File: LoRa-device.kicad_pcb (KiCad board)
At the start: 2 copper layers, 86.4 x 50.8 mm, 90 parts, among them J1 USB_C_Receptacle_USB2.0_14P, J2 Conn_01x02_Pin, J3 Conn_01x12_Pin, J4 Conn_01x14_Pin, J6 Conn_01x04_Pin, Q1 AO3401A, Q2 S8050, U1 ESP32-S3, U2 W25Q128JVS, U3 MCP73831-2-OT, U4 AMS1117-3.3, U5 Ai-Thinker-Ra-01, U6 BME280, U7 L70-R, Y1 32.768 kHz, Y2 40MHz(10ppm)

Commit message: First routing
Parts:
- removed C1: 100nF, PCM_JLCPCB:C_0402
- removed C5, C9: 15pF, Capacitor_SMD:C_0402_1005Metric
- removed U6: BME280, PCM_JLCPCB:Bosch_LGA-8_2.5x2.5mm_P0.65mm_ClockwisePinNumbering
- added DNP4: ~, Capacitor_SMD:C_0402_1005Metric, F.Cu at (163.7, 75.8)
- added DNP5: ~, Capacitor_SMD:C_0402_1005Metric, F.Cu at (176.2, 119.8)
- added Q3: AO3401A, Package_TO_SOT_SMD:SOT-23, F.Cu at (112.5, 113.7)
- added R7: 100kΩ, PCM_JLCPCB:R_0402, F.Cu at (115.2, 113.7)
- added SW1: SW_Nidec_CAS-120A1, Connector_PinSocket_2.54mm:PinSocket_1x03_P2.54mm_Vertical, F.Cu at (185.7, 114.9)
- DNP2, DNP3: value 15pF -> ~
- moved Q2 27.4 mm to (173.5, 103.7)
- moved D5 27.4 mm to (179.5, 103.7)
- moved R5 27.4 mm to (170.4, 103.3)
- moved BZ1 26.1 mm to (176.6, 111.7)
- moved DNP3 16.0 mm to (157.2, 114.6), turned to 180 degrees
- moved L4 15.6 mm to (160.7, 117.0), turned to 180 degrees
- moved R4 15.6 mm to (159.6, 114.6)
- moved R6 13.8 mm to (161.4, 115.0), turned to 90 degrees
- moved R3 12.6 mm to (165.7, 114.9), turned to -90 degrees
- moved DNP2 12.4 mm to (163.7, 78.5)
- moved L1 12.3 mm to (166.2, 77.2)
- moved U7 6.97 mm to (161.4, 107.2), turned to -90 degrees
- moved R25 4.97 mm to (116.7, 82.1), turned to 180 degrees
- moved R24 4.27 mm to (141.2, 89.7), turned to 0 degrees
- moved J3 4.25 mm to (141.6, 121.8)
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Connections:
- C7 pad 1: VSYS -> VSYS_SW
- J3 pad 3: VDD_CPU -> GND
- J3 pad 4: GND -> IO37
- U4 pad 3: VSYS -> VSYS_SW
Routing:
- net Net-(Q3-G): track 0.00 -> 87.5 mm, vias 0 -> 2
- net IO7: track 0.00 -> 85.9 mm, vias 0 -> 4
- net IO35: track 0.00 -> 64.4 mm, vias 0 -> 4
- net IO21: track 0.00 -> 57.4 mm, vias 0 -> 2
- net IO36: track 0.00 -> 54.9 mm, vias 0 -> 4
- net IO34: track 0.00 -> 41.8 mm, vias 0 -> 2
- net RX: track 0.00 -> 41.8 mm, vias 0 -> 4
- net VSYS_SW: track 0.00 -> 34.9 mm, vias 0 -> 2
- net IO14/SCK: track 171.6 -> 141.0 mm, vias 10 -> 9
- net IO46: track 80.1 -> 50.1 mm, vias 9 -> 3
- net IO0: track 14.7 -> 41.4 mm, vias 2 -> 4
- net IO5: track 40.7 -> 65.1 mm
- net Net-(U5-ANT): track 29.8 -> 5.93 mm, vias 2 -> 0
- net SPICS0: track 0.00 -> 23.8 mm, vias 0 -> 4
- net IO39: track 56.3 -> 77.0 mm, vias 2 -> 3
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
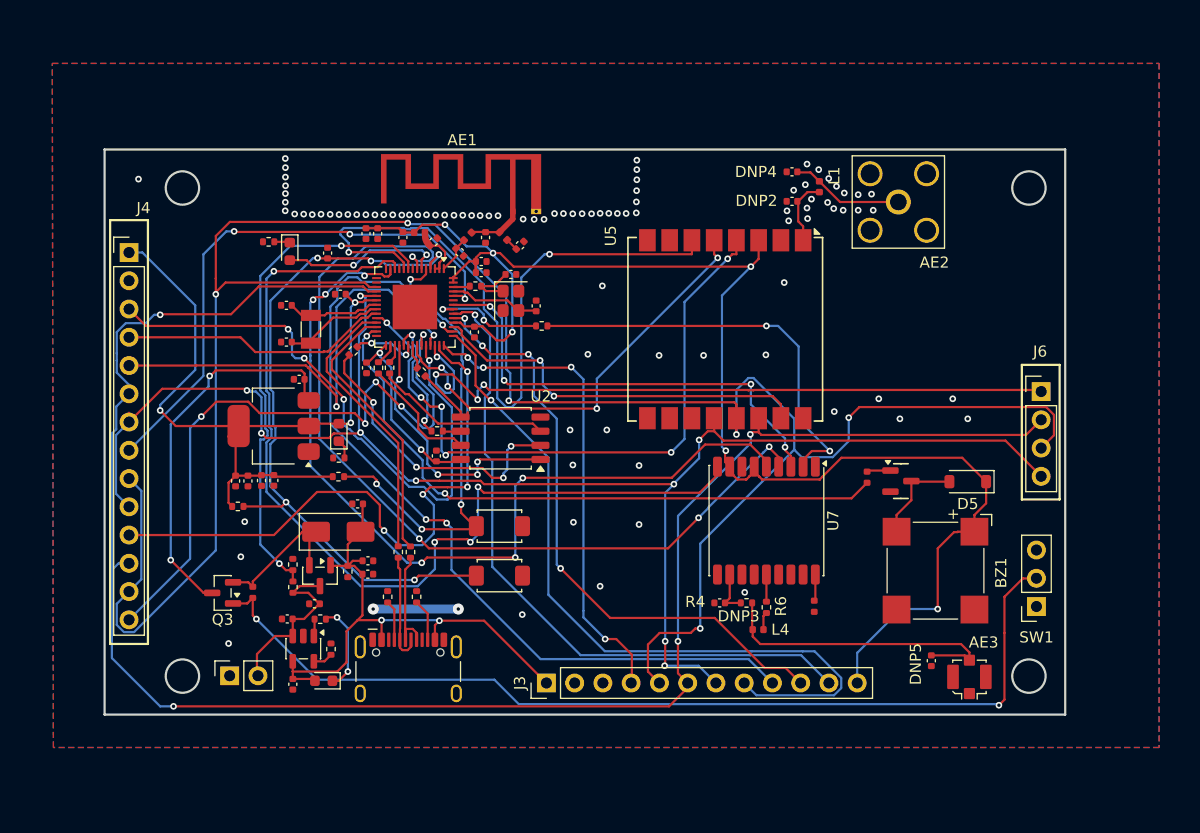
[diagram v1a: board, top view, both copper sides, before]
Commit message: Completed routing
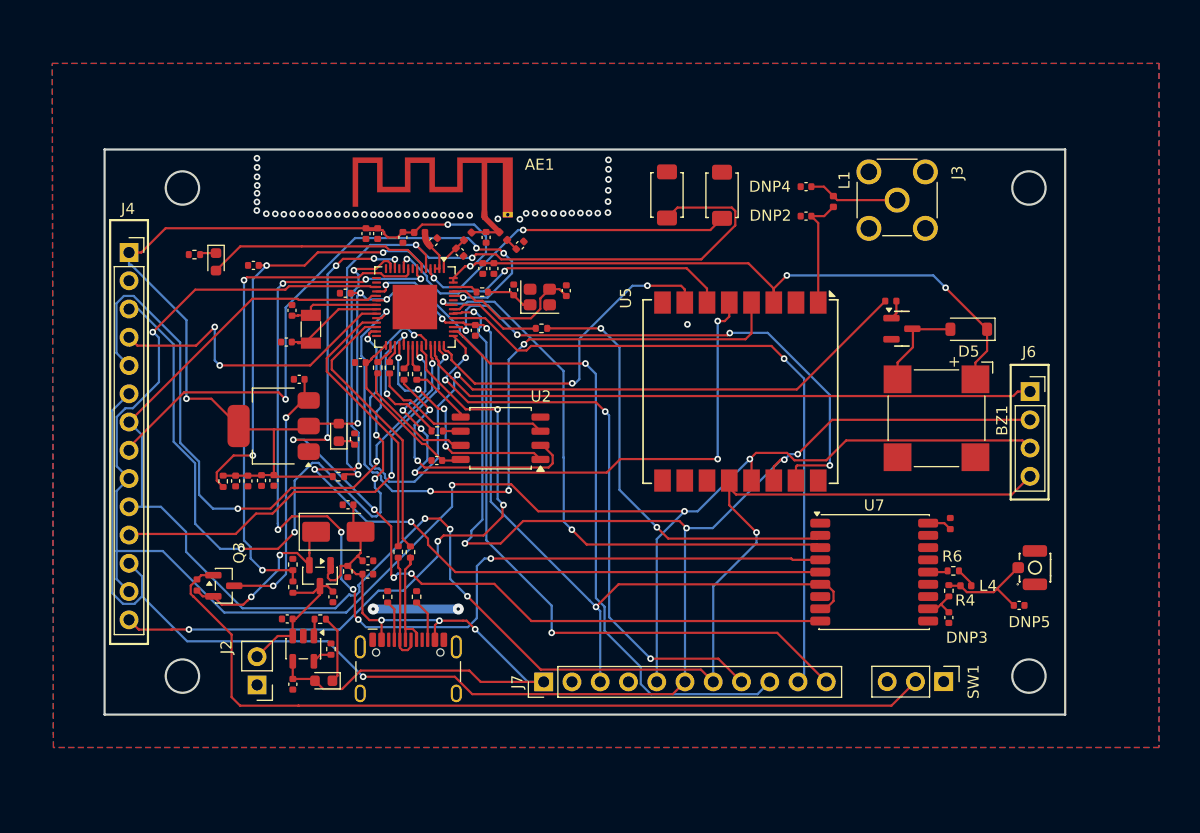
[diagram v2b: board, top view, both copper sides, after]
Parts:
- removed AE2: Antenna, Connector_Coaxial:SMA_Amphenol_132203-12_Horizontal
- removed AE3: Antenna, Connector_Coaxial:U.FL_Molex_MCRF_73412-0110_Vertical
- removed Flash1, Reset1: Tactile Button, 160gf, PCM_JLCPCB:SW_TS-1088-AR02016
- added FLASH1: Tactile Button, 160gf, PCM_JLCPCB:SW_TS-1088-AR02016, F.Cu at (152.5, 77.9)
- added J5: U.FL, PCM_JLCPCB:IPEX-SMD_BWIPX-1-001E, F.Cu at (184.8, 111.4)
- added J7: Conn_01x11_Pin, Connector_PinHeader_2.54mm:PinHeader_1x11_P2.54mm_Vertical, F.Cu at (141.4, 121.7)
- added RESET1: Tactile Button, 160gf, PCM_JLCPCB:SW_TS-1088-AR02016, F.Cu at (157.4, 78.0)
- J2: footprint Connector_PinSocket_2.54mm:PinSocket_1x02_P2.54mm_Vertical -> Connector_PinHeader_2.54mm:PinHeader_1x02_P2.54mm_Vertical
- J3: value Conn_01x12_Pin -> Conn_Coaxial; footprint Connector_PinHeader_2.54mm:PinHeader_1x12_P2.54mm_Vertical -> Connector_Coaxial:SMA_Molex_73251-2200_Horizontal
- J4: footprint Connector_PinHeader_2.54mm:PinHeader_1x14_P2.54mm_Vertical -> Connector_PinSocket_2.54mm:PinSocket_1x14_P2.54mm_Vertical
- J6: footprint Connector_PinHeader_2.54mm:PinHeader_1x04_P2.54mm_Vertical -> Connector_PinSocket_2.54mm:PinSocket_1x04_P2.54mm_Vertical
- SW1: footprint Connector_PinSocket_2.54mm:PinSocket_1x03_P2.54mm_Vertical -> Connector_PinHeader_2.54mm:PinHeader_1x03_P2.54mm_Vertical
- moved J3 53.7 mm to (173.2, 78.4), turned to 0 degrees
- moved DNP3 20.6 mm to (177.8, 115.9), turned to -90 degrees
- moved L4 19.1 mm to (179.3, 113.1)
- moved R4 18.2 mm to (177.8, 113.5), turned to 90 degrees
- moved R6 17.1 mm to (178.2, 111.7), turned to 180 degrees
- moved R5 16.0 mm to (172.6, 87.5), turned to 0 degrees
- moved R3 14.3 mm to (177.9, 107.5), turned to 90 degrees
- moved BZ1 13.7 mm to (176.7, 98.0)
- moved D5 13.7 mm to (179.6, 90.0)
- moved Q2 13.7 mm to (173.6, 90.0)
- moved U7 10.7 mm to (171.1, 111.8), turned to 0 degrees
- moved SW1 10.7 mm to (177.3, 121.7), turned to -90 degrees
- moved DNP5 9.33 mm to (184.1, 114.8), turned to 0 degrees
- moved R25 6.77 mm to (110.0, 83.3)
- moved C15 6.76 mm to (115.3, 84.3), turned to 180 degrees
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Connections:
- DNP4 pad 1: Net-(AE2-FEED) -> Net-(J3-In)
- J3 pad 1: 5V -> Net-(J3-In)
- L1 pad 2: Net-(AE2-FEED) -> Net-(J3-In)
- U5 pad 7: unconnected-(U5-DIO2-Pad7) -> IO37
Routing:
- net IO12/MISO: track 205.7 -> 161.9 mm, vias 6 -> 4
- net IO5: track 65.1 -> 32.5 mm
- net VDD_CPU: track 203.5 -> 233.3 mm, vias 9 -> 11
- net IO0: track 41.4 -> 68.6 mm, vias 4 -> 3
- net IO39: track 77.0 -> 56.4 mm, vias 3 -> 1
- net IO2: track 80.4 -> 98.6 mm, vias 4 -> 8
- net Net-(J5-In): track 27.4 -> 9.53 mm
- net IO48: track 39.6 -> 57.0 mm, vias 4 -> 6
- net IO34: track 41.8 -> 59.2 mm, vias 2 -> 3
- net IO33: track 53.3 -> 69.2 mm, vias 4 -> 5
- net IO40: track 35.0 -> 50.2 mm, vias 2 -> 4
- net IO36: track 54.9 -> 39.7 mm, vias 4 -> 2
- net IO13/MOSI: track 166.2 -> 181.2 mm, vias 4 -> 6
- net IO21: track 57.4 -> 71.4 mm
- net IO14/SCK: track 141.0 -> 154.6 mm, vias 9 -> 4
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
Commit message: Major rerouting and ESD protection for USB port
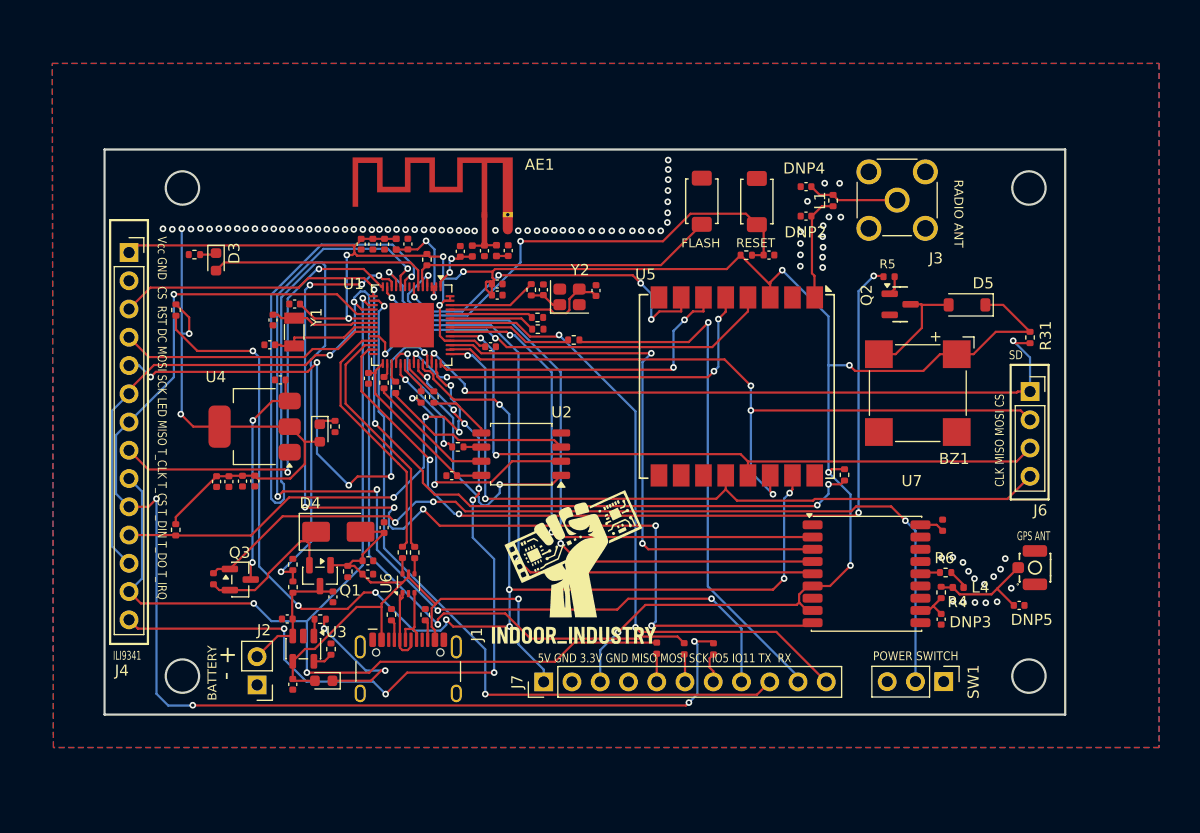
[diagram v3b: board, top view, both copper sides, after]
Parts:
- removed C36: 10uF, Capacitor_SMD:C_0402_1005Metric
- added C1: 1uF, Capacitor_SMD:C_0402_1005Metric, F.Cu at (118.8, 121.9)
- added G***: LOGO, LOGO, F.Cu at (144.1, 112.7)
- added R10: 10K, Resistor_SMD:R_0402_1005Metric, F.Cu at (168.4, 103.1)
- added R11: 10K, Resistor_SMD:R_0402_1005Metric, F.Cu at (108.3, 108.0)
- added R13: 10K, Resistor_SMD:R_0402_1005Metric, F.Cu at (108.3, 88.3)
- added R31: 10K, Resistor_SMD:R_0402_1005Metric, F.Cu at (185.1, 90.7)
- added R32: 10Ω, PCM_JLCPCB:R_0402, F.Cu at (151.5, 118.7)
- added R33: 10Ω, PCM_JLCPCB:R_0402, F.Cu at (154.0, 118.7)
- added R34: 10Ω, PCM_JLCPCB:R_0402, F.Cu at (156.6, 118.7)
- added R8: 10K, Resistor_SMD:R_0402_1005Metric, F.Cu at (140.8, 90.0)
- added R9: 10K, Resistor_SMD:R_0402_1005Metric, F.Cu at (140.8, 88.9)
- added U6: USBLC6-2P6, Package_TO_SOT_SMD:SOT-666, F.Cu at (129.2, 112.8)
- DNP1: value 15pF -> ~
- L1: value 4.7nH -> 0R; footprint Inductor_SMD:L_0402_1005Metric -> Resistor_SMD:R_0402_1005Metric
- U3: value MCP73831-2-OT -> TP4055
- moved R22 51.2 mm to (159.6, 83.3), turned to 180 degrees
- moved C15 46.4 mm to (161.6, 83.3), turned to 0 degrees
- moved R21 21.1 mm to (130.9, 83.7), turned to -90 degrees
- moved C10 4.65 mm to (119.0, 87.7)
- moved R23 4.41 mm to (140.3, 86.5), turned to 90 degrees
- moved C22 3.83 mm to (127.0, 107.8), turned to 90 degrees
- moved FLASH1 3.18 mm to (155.6, 78.5)
- moved RESET1 3.18 mm to (160.5, 78.5)
- moved R24 3.08 mm to (144.1, 91.0)
- moved BZ1 2.82 mm to (175.0, 95.7)
- moved C40 2.72 mm to (137.2, 86.9), turned to 0 degrees
- moved C33 2.67 mm to (146.1, 86.5)
- moved C4 2.67 mm to (141.3, 86.5)
- moved Y2 2.67 mm to (143.7, 87.1)
- moved R26 2.57 mm to (131.5, 96.1)
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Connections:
- C17 pad 1: VDD_CPU -> GND
- C20 pad 1: VDD_CPU -> GND
- C3 pad 1: VDD_CPU -> GND
- C35 pad 1: VDD_CPU -> GND
- D2 pad 2: VDD_CPU -> GND
- J1 pad A6: USB_D+ -> Net-(J1-D+-PadA6)
- J1 pad A7: USB_D- -> Net-(J1-D--PadA7)
- J1 pad B6: USB_D+ -> Net-(J1-D+-PadA6)
- J1 pad B7: USB_D- -> Net-(J1-D--PadA7)
- J4 pad 10: IO14/SCK -> SCKB
- J4 pad 12: IO13/MOSI -> MOSIB
- J4 pad 13: IO12/MISO -> MISOB
- J4 pad 3: IO33 -> IO10
- J4 pad 6: IO13/MOSI -> MOSIB
- J4 pad 7: IO14/SCK -> SCKB
- J4 pad 8: IO46 -> IO9
- J4 pad 9: IO12/MISO -> MISOB
- J6 pad 2: IO13/MOSI -> MOSIA
- J6 pad 3: IO12/MISO -> MISOA
- J6 pad 4: IO14/SCK -> SCKA
- J7 pad 10: IO41 -> TX
- J7 pad 11: IO42 -> RX
- J7 pad 5: IO12/MISO -> Net-(J7-Pin_5)
- J7 pad 6: IO13/MOSI -> Net-(J7-Pin_6)
- J7 pad 7: IO14/SCK -> Net-(J7-Pin_7)
- J7 pad 8: IO38 -> IO5
- J7 pad 9: IO39 -> IO11
- R18 pad 1: USB_D+ -> Net-(R18-Pad1)
- R2 pad 1: USB_D- -> Net-(R2-Pad1)
- U1 pad 17: IO12/MISO -> MISOB
- U1 pad 18: IO13/MOSI -> MOSIB
- U1 pad 19: IO14/SCK -> SCKB
- U1 pad 43: IO38 -> SCKA
- U1 pad 44: IO39 -> MOSIA
- U1 pad 47: IO41 -> MISOA
- U1 pad 8: IO3 -> unconnected-(U1-GPIO3-Pad8)
- U4 pad 2: VDD_CPU -> GND
- U5 pad 12: IO14/SCK -> SCKA
- U5 pad 13: IO12/MISO -> MISOA
- U5 pad 14: IO13/MOSI -> MOSIA
- U5 pad 15: IO40 -> IO33
- U5 pad 6: IO5 -> IO37
- U5 pad 7: IO37 -> IO2
- U7 pad 2: TX -> IO42
- U7 pad 3: RX -> IO40
- U7 pad 4: IO2 -> IO6
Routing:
- net IO13/MOSI: track 181.2 -> 0.00 mm, vias 6 -> 0
- net IO12/MISO: track 161.9 -> 0.00 mm, vias 4 -> 0
- net IO14/SCK: track 154.6 -> 0.00 mm, vias 4 -> 0
- net SCKB: track 0.00 -> 116.8 mm, vias 0 -> 5
- net MOSIB: track 0.00 -> 102.3 mm, vias 0 -> 3
- net MISOB: track 0.00 -> 97.8 mm, vias 0 -> 3
- net IO10: track 0.00 -> 83.7 mm, vias 0 -> 4
- net SCKA: track 0.00 -> 67.3 mm, vias 0 -> 2
- net IO2: track 98.6 -> 31.4 mm, vias 8 -> 4
- net IO11: track 0.00 -> 66.3 mm, vias 0 -> 2
- net MOSIA: track 0.00 -> 66.2 mm, vias 0 -> 3
- net MISOA: track 0.00 -> 64.0 mm, vias 0 -> 2
- net IO41: track 61.6 -> 0.00 mm, vias 1 -> 0
- net IO6: track 0.00 -> 60.2 mm, vias 0 -> 2
- net IO5: track 32.5 -> 90.2 mm, vias 2 -> 5
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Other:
- board text added: "+ -"
- board text added: "5V GND 3.3V GND MISO MOSI SCK IO5 IO11 TX RX"
- board text added: "BATTERY"
- board text added: "CLK MISO MOSI CS"
- board text added: "FLASH"
- board text added: "GPS ANT"
- board text added: "ILI9341"
- board text added: "POWER SWITCH"
- board text added: "RADIO ANT"
- board text added: "RESET"
- board text added: "SD"
- board text added: "Vcc GND CS RST DC MOSI SCK LED MISO T_CLK T_CS T_DIN T_DO T_IRQ"

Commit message: Routing complete, case work begins
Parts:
- moved R11 4.41 mm to (109.6, 103.8)
- moved C16 1.21 mm to (126.7, 111.7), turned to 180 degrees
- moved C6 1.21 mm to (126.8, 110.5), turned to 180 degrees
- moved G*** 0.80 mm to (143.9, 112.0)
- moved R24 0.79 mm to (143.7, 90.3)
- moved R32 0.76 mm to (150.9, 118.2), turned to 180 degrees
- moved R33 0.75 mm to (153.4, 118.2), turned to 180 degrees
- moved R20 0.66 mm to (123.6, 111.1)
- moved C4 0.62 mm to (141.4, 87.1)
- moved R23 0.61 mm to (140.3, 87.1)
- moved R34 0.54 mm to (156.7, 118.2), turned to 180 degrees
- moved C32 0.52 mm to (133.6, 103.1)
- moved R13 0.39 mm to (108.7, 88.2), turned to 180 degrees
- moved C11 0.25 mm to (136.7, 91.8)
- moved C39 0.22 mm to (137.4, 85.8)
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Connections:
- C17 pad 1: GND -> VDD_CPU
- C20 pad 1: GND -> VDD_CPU
- C3 pad 1: GND -> VDD_CPU
- C35 pad 1: GND -> VDD_CPU
- D2 pad 2: GND -> VDD_CPU
- R10 pad 2: IO10 -> IO33
- R11 pad 1: GND -> VDD_CPU
- R13 pad 1: GND -> VDD_CPU
- R13 pad 2: IO33 -> IO10
- U4 pad 2: GND -> VDD_CPU
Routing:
- net IO33: track 119.6 -> 47.1 mm, vias 9 -> 2
- net IO10: track 83.7 -> 28.6 mm, vias 4 -> 0
- net GND: track 51.8 -> 1.39 mm, vias 91 -> 89
- net VDD_CPU: track 184.3 -> 232.3 mm, vias 10 -> 12
- net IO21: track 78.4 -> 90.2 mm
- net TX: track 48.1 -> 41.7 mm
- net 5V: track 57.9 -> 53.4 mm
- net IO48: track 35.9 -> 39.9 mm
- net IO40: track 51.3 -> 47.7 mm
- net IO37: track 29.2 -> 32.7 mm
- net VSYS: track 14.0 -> 17.1 mm
- net IO2: track 31.4 -> 28.6 mm, vias 4 -> 2
- net IO7: track 87.5 -> 84.8 mm
- net IO18: track 39.1 -> 37.1 mm
- net EN: track 45.4 -> 44.0 mm, vias 2 -> 4
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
